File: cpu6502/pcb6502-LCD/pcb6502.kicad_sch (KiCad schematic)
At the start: 45 parts, among them J1 Power, J2 RS232, SW1 Reset, SW2 IRQ, SW3 Debug, U1 6502 (CPU), U2 28C256 (ROM), U3 62256 (RAM), U4 6522 (VIA), U5 74HC00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

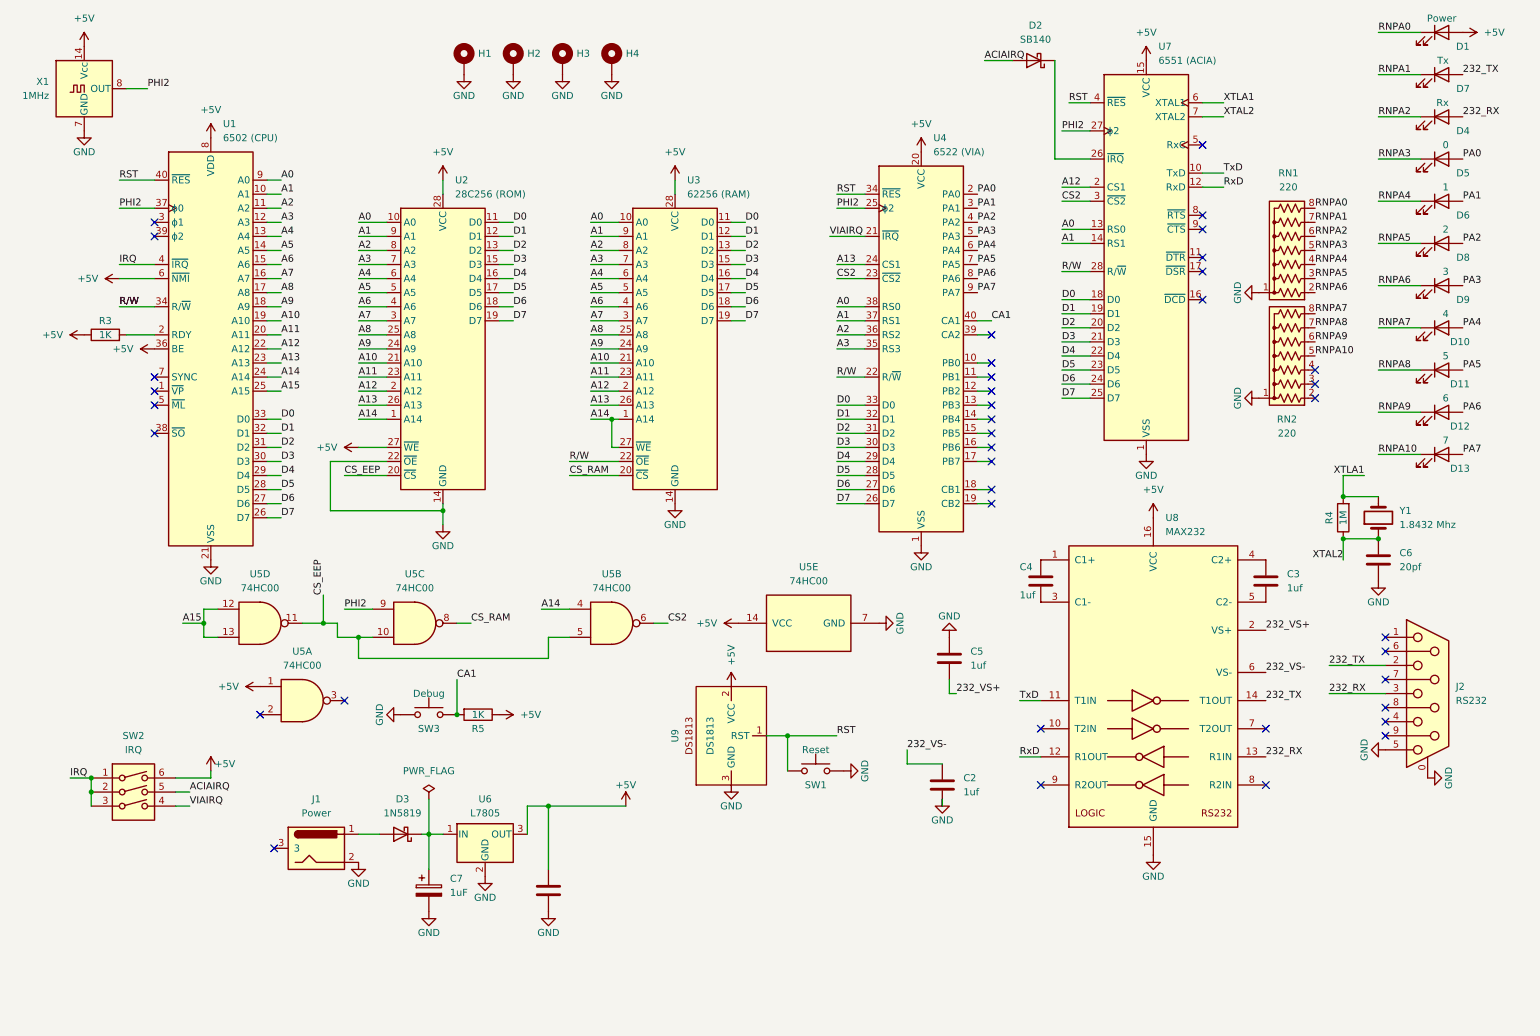
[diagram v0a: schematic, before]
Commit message: PCB 99.9999% ready to be built (without LCD)
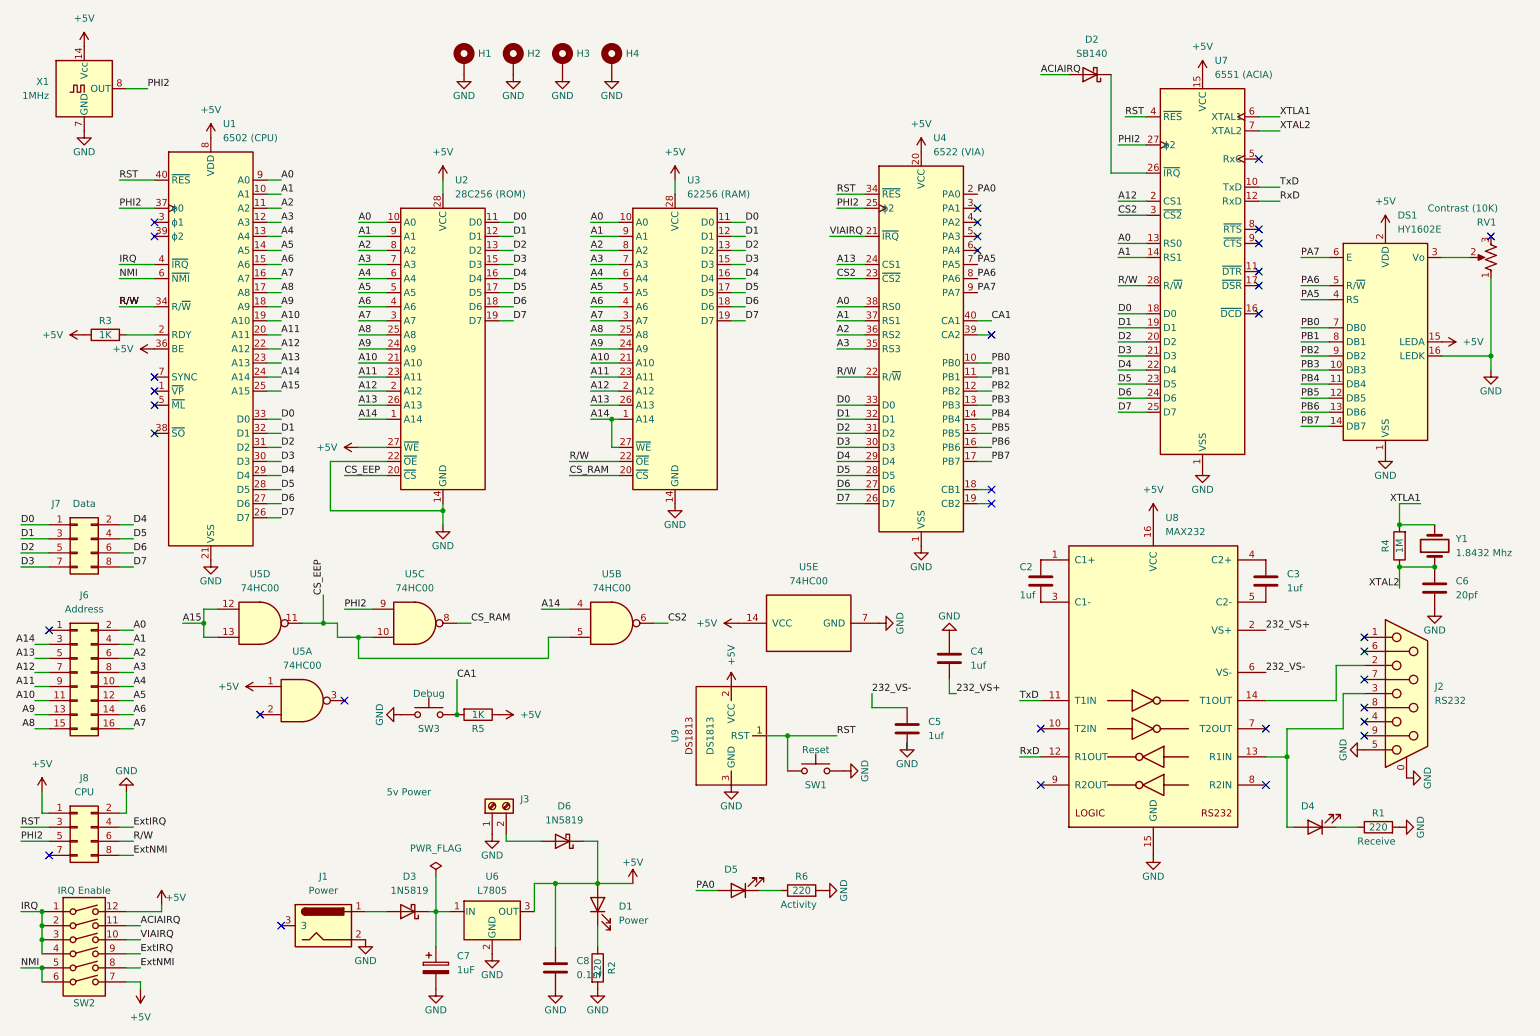
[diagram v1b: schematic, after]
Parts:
- removed D10: 4, LED_THT:LED_D3.0mm, symbol Device:LED
- removed D11: 5, LED_THT:LED_D3.0mm, symbol Device:LED
- removed D12: 6, LED_THT:LED_D3.0mm, symbol Device:LED
- removed D13: 7, LED_THT:LED_D3.0mm, symbol Device:LED
- removed D6: 1, LED_THT:LED_D3.0mm, symbol Device:LED
- removed D7: Tx, LED_THT:LED_D3.0mm, symbol Device:LED
- removed D8: 2, LED_THT:LED_D3.0mm, symbol Device:LED
- removed D9: 3, LED_THT:LED_D3.0mm, symbol Device:LED
- removed RN1, RN2: 220, Resistor_THT:R_Array_SIP8, symbol Device:R_Network07_US
- removed SW2: IRQ, Button_Switch_THT:SW_DIP_SPSTx03_Slide_9.78x9.8mm_W7.62mm_P2.54mm, symbol Switch:SW_DIP_x03
- added D6: 1N5819, Diode_THT:D_DO-41_SOD81_P10.16mm_Horizontal, symbol Diode:1N5819
- added DS1: HY1602E, Display:WC1602A, symbol Display_Character:HY1602E
- added J3: 5v Power, TerminalBlock_TE-Connectivity:TerminalBlock_TE_282834-2_1x02_P2.54mm_Horizontal, symbol Connector:Screw_Terminal_01x02
- added J6: Address, Connector_PinHeader_2.54mm:PinHeader_2x08_P2.54mm_Vertical, symbol Connector_Generic:Conn_02x08_Odd_Even
- added J7: Data, Connector_PinHeader_2.54mm:PinHeader_2x04_P2.54mm_Vertical, symbol Connector_Generic:Conn_02x04_Odd_Even
- added J8: CPU, Connector_PinHeader_2.54mm:PinHeader_2x04_P2.54mm_Vertical, symbol Connector_Generic:Conn_02x04_Odd_Even
- added R1, R2, R6: 220, Resistor_THT:R_Axial_DIN0204_L3.6mm_D1.6mm_P7.62mm_Horizontal, symbol Device:R
- added RV1: Contrast (10K), Potentiometer_THT:Potentiometer_Bourns_3386P_Vertical, symbol Device:R_Potentiometer_US
- added SW2: IRQ Enable, Button_Switch_THT:SW_DIP_SPSTx06_Slide_6.7x16.8mm_W7.62mm_P2.54mm_LowProfile, symbol Switch:SW_DIP_x06
- D1: footprint LED_THT:LED_D3.0mm -> LED_THT:LED_D5.0mm
- D4: value Rx -> Receive; footprint LED_THT:LED_D3.0mm -> LED_THT:LED_D5.0mm
- D5: value 0 -> Activity; footprint LED_THT:LED_D3.0mm -> LED_THT:LED_D5.0mm
- renumbered C4 to C2, C5 to C4, C2 to C5
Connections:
- net +5V: now also D6.1 (K), DS1.15 (LEDA), DS1.2 (VDD), J8.1 (Pin_1), SW2.12, SW2.7; no longer U1.6 (~{NMI})
- net A0: now also J6.2 (Pin_2)
- net A1: now also J6.4 (Pin_4)
- net A10: now also J6.11 (Pin_11)
- net A11: now also J6.9 (Pin_9)
- net A12: now also J6.7 (Pin_7)
- net A13: now also J6.5 (Pin_5)
- net A14: now also J6.3 (Pin_3)
- net A2: now also J6.6 (Pin_6)
- net A3: now also J6.8 (Pin_8)
- net A4: now also J6.10 (Pin_10)
- net A5: now also J6.12 (Pin_12)
- net A6: now also J6.14 (Pin_14)
- net A7: now also J6.16 (Pin_16)
- net A8: now also J6.15 (Pin_15)
- net A9: now also J6.13 (Pin_13)
- net ACIAIRQ: now also SW2.11
- net D0: now also J7.1 (Pin_1)
- net D1: now also J7.3 (Pin_3)
- net D2: now also J7.5 (Pin_5)
- net D3: now also J7.7 (Pin_7)
- net D4: now also J7.2 (Pin_2)
- net D5: now also J7.4 (Pin_4)
- net D6: now also J7.6 (Pin_6)
- net D7: now also J7.8 (Pin_8)
- net GND: now also DS1.1 (VSS), DS1.16 (LEDK), J3.1 (Pin_1), J8.2 (Pin_2), R1.2, R2.2, R6.2, RV1.1
- net IRQ: now also SW2.1, SW2.2, SW2.3, SW2.4
- net PA5: now also DS1.4 (RS)
- net PA6: now also DS1.5 (R/~{W})
- net PA7: now also DS1.6 (E)
- net PHI2: now also J8.5 (Pin_5)
- net RST: now also J8.3 (Pin_3)
- net R/W: now also J8.6 (Pin_6)
- net VIAIRQ: now also SW2.10
- net PB0: now reaches U4.10 (PB0)
- net PB0: now also DS1.7 (DB0)
- net PB1: now reaches U4.11 (PB1)
- net PB1: now also DS1.8 (DB1)
- net PB2: now reaches U4.12 (PB2)
- net PB2: now also DS1.9 (DB2)
- net PB3: now reaches U4.13 (PB3)
- net PB3: now also DS1.10 (DB3)
- net PB4: now reaches U4.14 (PB4)
- net PB4: now also DS1.11 (DB4)
- net PB5: now reaches U4.15 (PB5)
- net PB5: now also DS1.12 (DB5)
- net PB6: now reaches U4.16 (PB6)
- net PB6: now also DS1.13 (DB6)
- net PB7: now reaches U4.17 (PB7)
- net PB7: now also DS1.14 (DB7)
- net 232_RX: no longer names the net of D4.2 (A), J2.3, U8.13 (R1IN)
- net 232_TX: no longer names the net of J2.2, U8.14 (T1OUT)
- net PA1: no longer names the net of U4.3 (PA1)
- net PA2: no longer names the net of U4.4 (PA2)
- net PA3: no longer names the net of U4.5 (PA3)
- net PA4: no longer names the net of U4.6 (PA4)
- net RNPA0: no longer names the net of D1.1 (K)
- net RNPA0: now also R2.1
- net RNPA2: no longer names the net of D4.1 (K)
- net RNPA2: now also R1.1
- net RNPA3: no longer names the net of D5.1 (K)
- net RNPA3: now also R6.1
- new net: D6.2 (A), J3.2 (Pin_2)
- new net: DS1.3 (Vo), RV1.2
- new net ExtIRQ: J8.4 (Pin_4), SW2.9
- new net ExtNMI: J8.8 (Pin_8), SW2.8
- new net NMI: SW2.5, SW2.6, U1.6 (~{NMI})
- no-connect marks 39 -> 35
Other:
- moved on the sheet: C5, C6, C7, D1, D2, D3, D4, J1, J2, R4, U6, U7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
